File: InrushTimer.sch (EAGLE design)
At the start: 71 parts, among them IC2 TLC272D, IC3 4076N, IC6 555, Q2 TIP41C

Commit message: Updated values and topology on schematic.
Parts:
- removed C25: 10p, rcl:C-EUC0805K
- added R20: 10K, rcl:R-EU_0207/2V
- C15: value 10p -> 10p (DNF)
- C17, C8: value 100nF -> 100nF (DNF)
- C9: value 1nF -> 10nF
- R12: value 43K -> 200K
- R13: value 10K -> 100K
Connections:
- new net N$26: IC2A.+IN, R11.1, R20.2
- net HYST: no longer R11.1
- net N$7: now also R20.1; no longer IC2A.+IN
- net PEAK: no longer C25.1
- net ZERO: no longer C25.2
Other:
- moved on the sheet: R11
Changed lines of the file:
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@@
 <setting verticaltext="up"/>
 </settings>
-<grid distance="0.1" unitdist="inch" unit="inch" style="lines" multiple="1" display="yes" altdistance="0.01" altunitdist="inch" altunit="inch"/>
+<grid distance="0.1" unitdist="inch" unit="inch" style="lines" multiple="1" display="no" altdistance="0.01" altunitdist="inch" altunit="inch"/>
 <layers>
 <layer number="1" name="Top" color="4" fill="1" visible="no" active="no"/>
@@
 <part name="R10" library="rcl" deviceset="R-EU_" device="0207/10" value="9.1M"/>
 <part name="D5" library="diode" deviceset="1N4148" device="DO35-7"/>
-<part name="R12" library="rcl" deviceset="R-EU_" device="0207/2V" value="43K"/>
-<part name="R13" library="rcl" deviceset="R-EU_" device="0207/2V" value="10K"/>
+<part name="R12" library="rcl" deviceset="R-EU_" device="0207/2V" value="200K"/>
+<part name="R13" library="rcl" deviceset="R-EU_" device="0207/2V" value="100K"/>
 <part name="IC3" library="40xx" deviceset="4076" device="N"/>
 <part name="D6" library="diode" deviceset="DIODE-" device="DO41-10" value="1n4001"/>
@@
 <part name="R14" library="rcl" deviceset="R-EU_" device="0207/2V" value="22K"/>
 <part name="R19" library="rcl" deviceset="R-EU_" device="0207/2V" value="10K"/>
-<part name="C15" library="rcl" deviceset="C-EU" device="C0805K" value="10p"/>
+<part name="C15" library="rcl" deviceset="C-EU" device="C0805K" value="10p (DNF)"/>
 <part name="U$3" library="transistor-fet" deviceset="2N7002" device=""/>
 <part name="D12" library="diode" deviceset="BZX55" device=""/>
@@
 <part name="C4" library="rcl" deviceset="C-EU" device="050-024X044" value="100nF"/>
 <part name="C13" library="rcl" deviceset="C-EU" device="C1206K" value="100nF"/>
-<part name="C25" library="rcl" deviceset="C-EU" device="C0805K" value="10p"/>
 <part name="U$5" library="SHoleLib" deviceset="FODM3053" device=""/>
 <part name="Q2" library="transistor-power" deviceset="TIP41C" device=""/>
 <part name="R17" library="rcl" deviceset="R-EU_" device="R0805" value="1K"/>
 <part name="X6" library="con-wago-500" deviceset="W237-102" device=""/>
-<part name="C9" library="rcl" deviceset="C-EU" device="C0805K" value="1nF"/>
+<part name="C9" library="rcl" deviceset="C-EU" device="C0805K" value="10nF"/>
 <part name="C14" library="rcl" deviceset="C-EU" device="050-024X044" value="10nF"/>
 <part name="C10" library="rcl" deviceset="C-EU" device="C0805K" value="1nF"/>
@@
 <part name="T2" library="transistor" deviceset="*-NPN-" device="SOT23-BEC" technology="MMBTA42LT1"/>
 <part name="R2" library="rcl" deviceset="R-EU_" device="0207/2V" value="10K"/>
-<part name="C8" library="rcl" deviceset="C-EU" device="050-024X044" value="100nF"/>
-<part name="C17" library="rcl" deviceset="C-EU" device="050-024X044" value="100nF"/>
+<part name="C8" library="rcl" deviceset="C-EU" device="050-024X044" value="100nF (DNF)"/>
+<part name="C17" library="rcl" deviceset="C-EU" device="050-024X044" value="100nF (DNF)"/>
 <part name="R9" library="rcl" deviceset="R-EU_" device="0207/2V" value="10K"/>
 <part name="R16" library="rcl" deviceset="R-EU_" device="0207/2V" value="10K"/>
@@
 <part name="R5" library="rcl" deviceset="R-EU_" device="0207/2V" value="10K"/>
 <part name="R18" library="rcl" deviceset="R-EU_" device="0207/2V" value="100"/>
+<part name="R20" library="rcl" deviceset="R-EU_" device="0207/2V" value="10K"/>
 </parts>
 <sheets>
@@
 <instance part="IC3" gate="P" x="335.28" y="-12.7"/>
 <instance part="D6" gate="G$1" x="99.06" y="116.84" rot="R90"/>
-<instance part="R11" gate="G$1" x="187.96" y="127" rot="R90"/>
+<instance part="R11" gate="G$1" x="177.8" y="152.4"/>
 <instance part="U$4" gate="G$1" x="50.8" y="-22.86"/>
 <instance part="R7" gate="G$1" x="-2.54" y="2.54" rot="R270"/>
@@
 <instance part="C4" gate="G$1" x="78.74" y="40.64"/>
 <instance part="C13" gate="G$1" x="132.08" y="106.68"/>
-<instance part="C25" gate="G$1" x="208.28" y="119.38"/>
 <instance part="U$5" gate="G$1" x="518.16" y="27.94"/>
 <instance part="Q2" gate="1" x="83.82" y="50.8"/>
@@
 <instance part="R5" gate="G$1" x="388.62" y="7.62" rot="R180"/>
 <instance part="R18" gate="G$1" x="71.12" y="-20.32" rot="R180"/>
+<instance part="R20" gate="G$1" x="154.94" y="139.7"/>
 </instances>
 <busses>
@@
 <segment>
 <pinref part="R12" gate="G$1" pin="1"/>
-<wire x1="154.94" y1="129.54" x2="154.94" y2="137.16" width="0.1524" layer="91"/>
-<label x="154.94" y="132.08" size="1.778" layer="95" rot="R90"/>
+<wire x1="154.94" y1="129.54" x2="154.94" y2="132.08" width="0.1524" layer="91"/>
+<label x="144.78" y="132.08" size="1.778" layer="95"/>
+<wire x1="154.94" y1="132.08" x2="144.78" y2="132.08" width="0.1524" layer="91"/>
 </segment>
 <segment>
@@
 <junction x="99.06" y="99.06"/>
 <pinref part="C15" gate="G$1" pin="2"/>
-<wire x1="200.66" y1="114.3" x2="200.66" y2="109.22" width="0.1524" layer="91"/>
-<wire x1="200.66" y1="109.22" x2="200.66" y2="99.06" width="0.1524" layer="91"/>
+<wire x1="200.66" y1="114.3" x2="200.66" y2="99.06" width="0.1524" layer="91"/>
 <wire x1="200.66" y1="99.06" x2="154.94" y2="99.06" width="0.1524" layer="91"/>
 <pinref part="C13" gate="G$1" pin="2"/>
@@
 <wire x1="78.74" y1="109.22" x2="88.9" y2="109.22" width="0.1524" layer="91"/>
 <junction x="88.9" y="109.22"/>
-<pinref part="C25" gate="G$1" pin="2"/>
-<wire x1="208.28" y1="114.3" x2="208.28" y2="109.22" width="0.1524" layer="91"/>
-<wire x1="208.28" y1="109.22" x2="200.66" y2="109.22" width="0.1524" layer="91"/>
-<junction x="200.66" y="109.22"/>
 <pinref part="C9" gate="G$1" pin="1"/>
 <wire x1="88.9" y1="99.06" x2="78.74" y2="99.06" width="0.1524" layer="91"/>
@@
 </segment>
 <segment>
-<wire x1="200.66" y1="137.16" x2="187.96" y2="137.16" width="0.1524" layer="91"/>
+<wire x1="200.66" y1="137.16" x2="190.5" y2="137.16" width="0.1524" layer="91"/>
 <label x="226.06" y="139.7" size="1.778" layer="95" rot="R180"/>
+<pinref part="C15" gate="G$1" pin="1"/>
+<wire x1="190.5" y1="137.16" x2="182.88" y2="137.16" width="0.1524" layer="91"/>
+<wire x1="200.66" y1="121.92" x2="200.66" y2="137.16" width="0.1524" layer="91"/>
+<pinref part="IC2" gate="A" pin="OUT"/>
+<wire x1="200.66" y1="137.16" x2="226.06" y2="137.16" width="0.1524" layer="91"/>
 <pinref part="R11" gate="G$1" pin="2"/>
-<wire x1="187.96" y1="132.08" x2="187.96" y2="137.16" width="0.1524" layer="91"/>
-<pinref part="C15" gate="G$1" pin="1"/>
-<wire x1="200.66" y1="121.92" x2="200.66" y2="127" width="0.1524" layer="91"/>
-<pinref part="C25" gate="G$1" pin="1"/>
-<wire x1="200.66" y1="127" x2="200.66" y2="137.16" width="0.1524" layer="91"/>
-<wire x1="208.28" y1="121.92" x2="208.28" y2="127" width="0.1524" layer="91"/>
-<wire x1="208.28" y1="127" x2="200.66" y2="127" width="0.1524" layer="91"/>
-<junction x="200.66" y="127"/>
-<pinref part="IC2" gate="A" pin="OUT"/>
-<wire x1="187.96" y1="137.16" x2="182.88" y2="137.16" width="0.1524" layer="91"/>
-<junction x="187.96" y="137.16"/>
-<wire x1="200.66" y1="137.16" x2="226.06" y2="137.16" width="0.1524" layer="91"/>
+<wire x1="182.88" y1="152.4" x2="190.5" y2="152.4" width="0.1524" layer="91"/>
+<wire x1="190.5" y1="152.4" x2="190.5" y2="137.16" width="0.1524" layer="91"/>
+<junction x="190.5" y="137.16"/>
 </segment>
 </net>
@@
 <wire x1="154.94" y1="116.84" x2="165.1" y2="116.84" width="0.1524" layer="91"/>
 <wire x1="165.1" y1="134.62" x2="165.1" y2="116.84" width="0.1524" layer="91"/>
-<junction x="165.1" y="116.84"/>
-<pinref part="R11" gate="G$1" pin="1"/>
-<wire x1="187.96" y1="121.92" x2="187.96" y2="116.84" width="0.1524" layer="91"/>
-<wire x1="187.96" y1="116.84" x2="165.1" y2="116.84" width="0.1524" layer="91"/>
 <pinref part="IC2" gate="A" pin="-IN"/>
 <wire x1="167.64" y1="134.62" x2="165.1" y2="134.62" width="0.1524" layer="91"/>
@@
 <net name="N$7" class="0">
 <segment>
-<pinref part="IC2" gate="A" pin="+IN"/>
 <pinref part="D5" gate="G$1" pin="A"/>
 <wire x1="132.08" y1="124.46" x2="132.08" y2="129.54" width="0.1524" layer="91"/>
@@
 <wire x1="127" y1="129.54" x2="132.08" y2="129.54" width="0.1524" layer="91"/>
 <wire x1="127" y1="139.7" x2="132.08" y2="139.7" width="0.1524" layer="91"/>
-<wire x1="167.64" y1="139.7" x2="132.08" y2="139.7" width="0.1524" layer="91"/>
-<junction x="132.08" y="139.7"/>
 <pinref part="C7" gate="G$1" pin="2"/>
 <wire x1="124.46" y1="124.46" x2="127" y2="124.46" width="0.1524" layer="91"/>
 <wire x1="127" y1="124.46" x2="127" y2="129.54" width="0.1524" layer="91"/>
 <junction x="127" y="129.54"/>
+<pinref part="R20" gate="G$1" pin="1"/>
+<wire x1="132.08" y1="139.7" x2="149.86" y2="139.7" width="0.1524" layer="91"/>
+<junction x="132.08" y="139.7"/>
 </segment>
 </net>
@@
 </segment>
 </net>
+<net name="N$26" class="0">
+<segment>
+<pinref part="R20" gate="G$1" pin="2"/>
+<pinref part="IC2" gate="A" pin="+IN"/>
+<wire x1="160.02" y1="139.7" x2="165.1" y2="139.7" width="0.1524" layer="91"/>
+<pinref part="R11" gate="G$1" pin="1"/>
+<wire x1="165.1" y1="139.7" x2="167.64" y2="139.7" width="0.1524" layer="91"/>
+<wire x1="172.72" y1="152.4" x2="165.1" y2="152.4" width="0.1524" layer="91"/>
+<wire x1="165.1" y1="152.4" x2="165.1" y2="139.7" width="0.1524" layer="91"/>
+<junction x="165.1" y="139.7"/>
+</segment>
+</net>

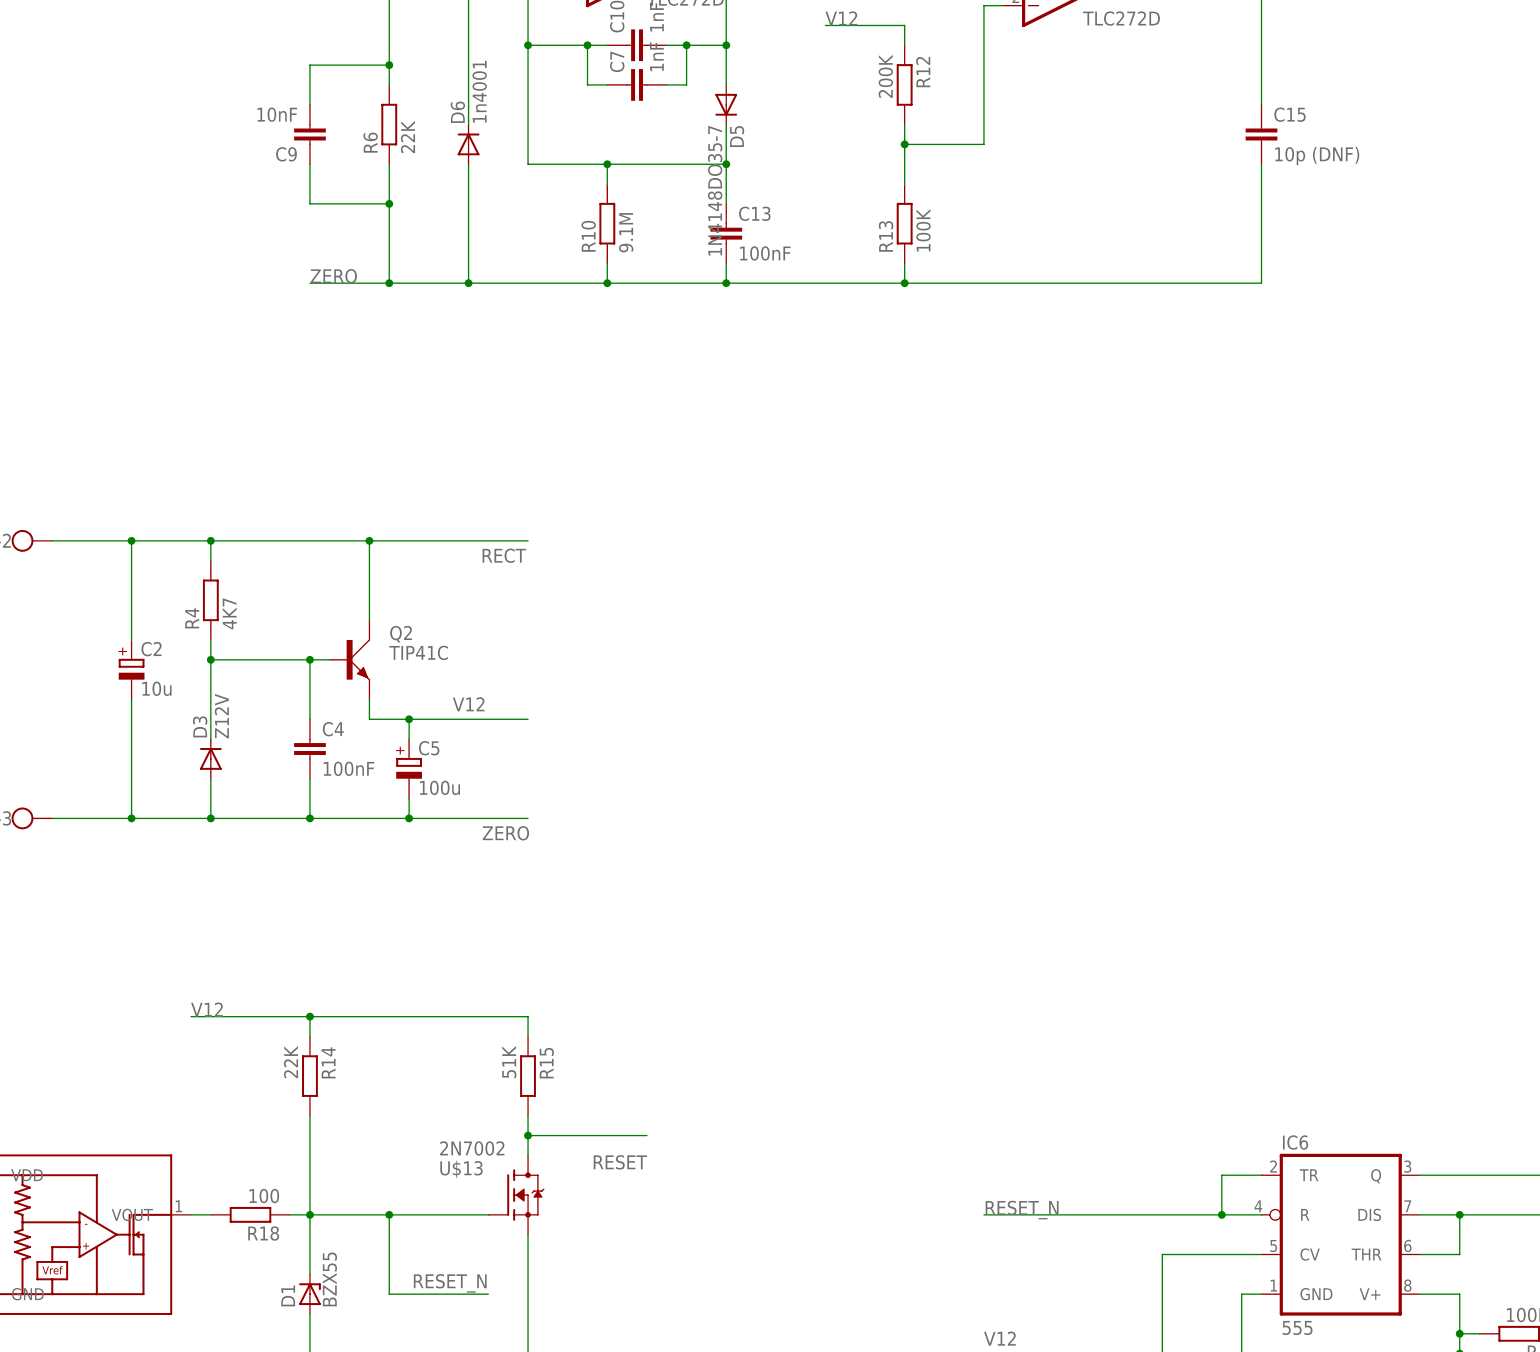
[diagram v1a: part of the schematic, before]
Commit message: Corrected component values (units)
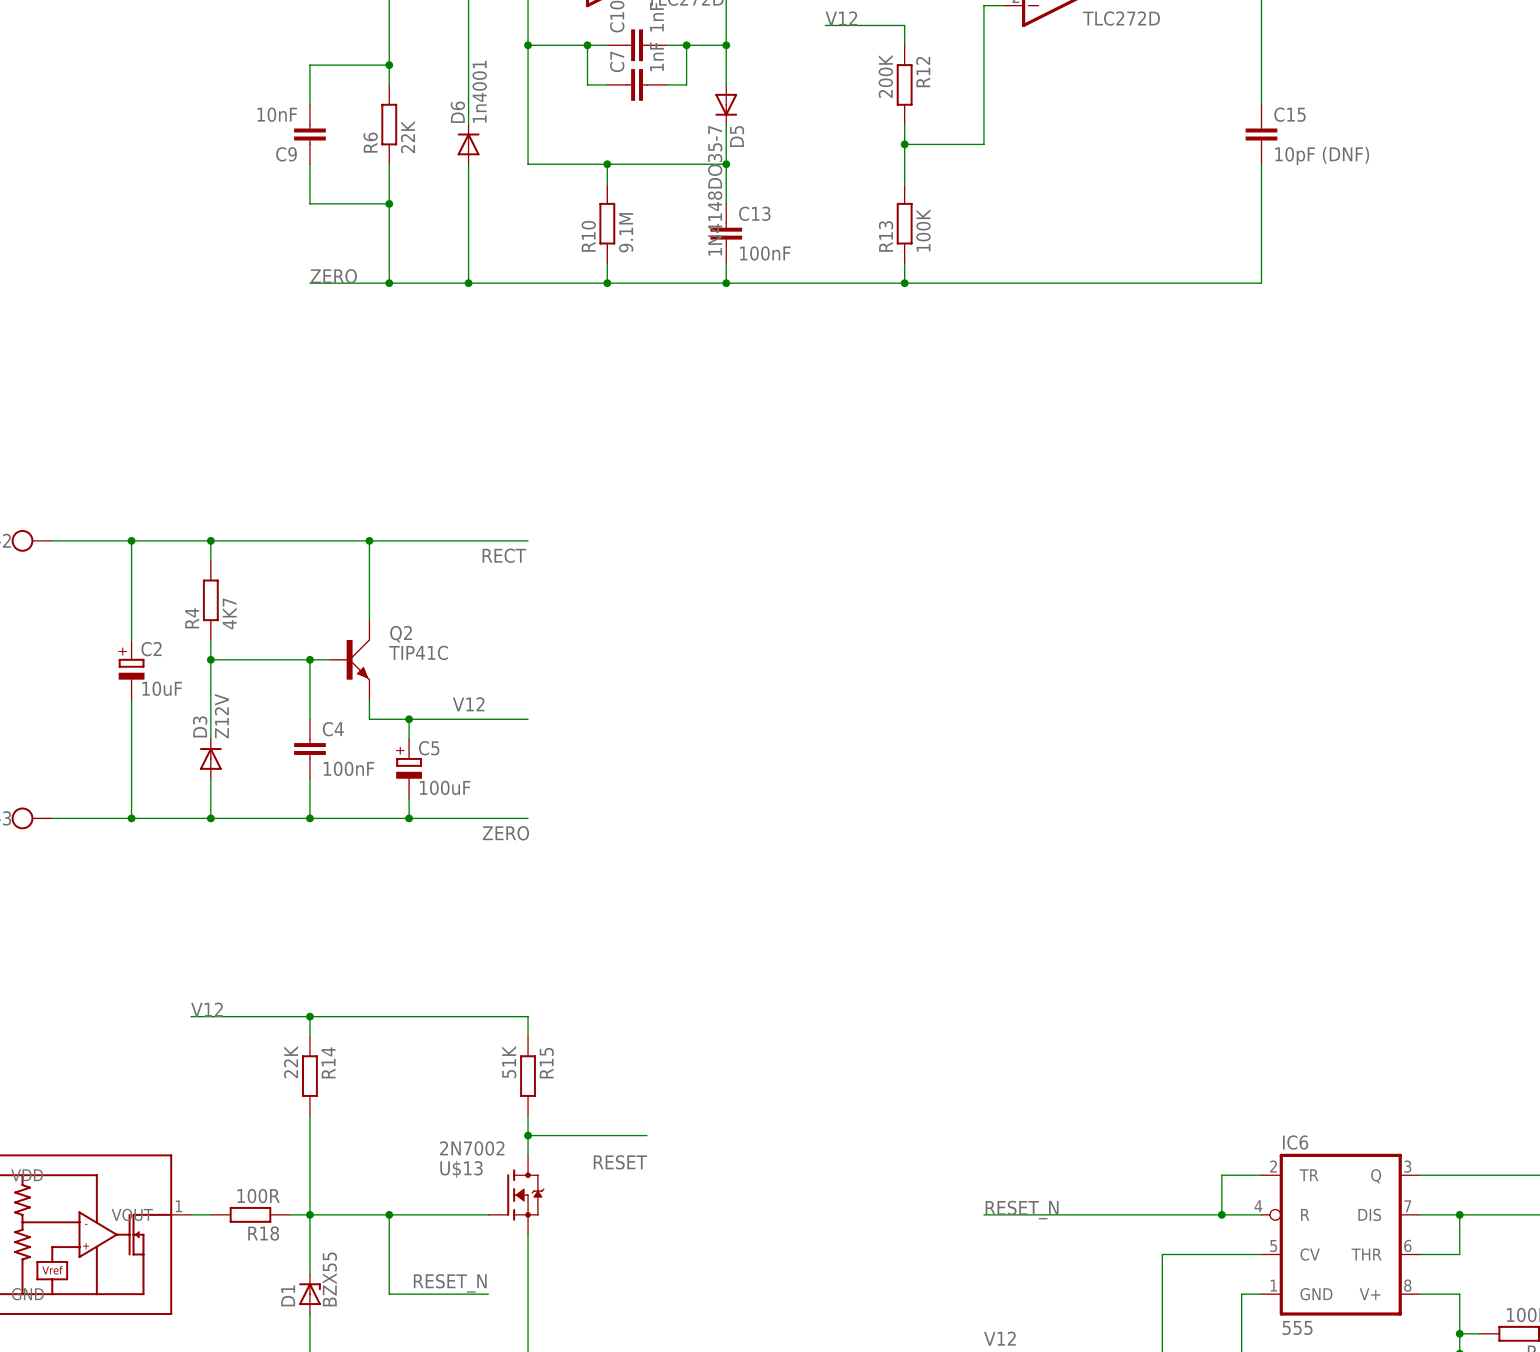
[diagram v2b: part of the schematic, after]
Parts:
- C15: value 10p (DNF) -> 10pF (DNF)
- C2: value 10u -> 10uF
- C5: value 100u -> 100uF
- R18: value 100 -> 100R
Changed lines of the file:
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@@
 <parts>
 <part name="D3" library="diode" deviceset="DIODE-" device="SOD323-R" value="Z12V"/>
-<part name="C2" library="rcl" deviceset="CPOL-EU" device="E2-5" value="10u"/>
-<part name="C5" library="rcl" deviceset="CPOL-EU" device="E2.5-7" value="100u"/>
+<part name="C2" library="rcl" deviceset="CPOL-EU" device="E2-5" value="10uF"/>
+<part name="C5" library="rcl" deviceset="CPOL-EU" device="E2.5-7" value="100uF"/>
 <part name="R4" library="rcl" deviceset="R-EU_" device="0207/2V" value="4K7"/>
 <part name="R6" library="rcl" deviceset="R-EU_" device="0207/2V" value="22K"/>
@@
 <part name="R14" library="rcl" deviceset="R-EU_" device="0207/2V" value="22K"/>
 <part name="R19" library="rcl" deviceset="R-EU_" device="0207/2V" value="10K"/>
-<part name="C15" library="rcl" deviceset="C-EU" device="C0805K" value="10p (DNF)"/>
+<part name="C15" library="rcl" deviceset="C-EU" device="C0805K" value="10pF (DNF)"/>
 <part name="U$3" library="transistor-fet" deviceset="2N7002" device=""/>
 <part name="D12" library="diode" deviceset="BZX55" device=""/>
@@
 <part name="R3" library="rcl" deviceset="R-EU_" device="0207/2V" value="10K"/>
 <part name="R5" library="rcl" deviceset="R-EU_" device="0207/2V" value="10K"/>
-<part name="R18" library="rcl" deviceset="R-EU_" device="0207/2V" value="100"/>
+<part name="R18" library="rcl" deviceset="R-EU_" device="0207/2V" value="100R"/>
 <part name="R20" library="rcl" deviceset="R-EU_" device="0207/2V" value="10K"/>
 </parts>
